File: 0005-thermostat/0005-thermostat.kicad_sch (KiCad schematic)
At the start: 41 parts, among them J1 EXT_NTC, J2 OUT, J3 PWR, J4 EXT_LED, J5 EXT_P1, J6 EXT_P2, P1 22k, P2 22k, T1 BC847B, T2 BC847B, T3 BC847B

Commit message: PCB enhancement
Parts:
- US1: footprint Package_DFN_QFN:DFN-8-1EP_2x2mm_P0.5mm_EP0.8x1.6mm -> Package_SO:SOP-8_3.76x4.96mm_P1.27mm
- US2: footprint Package_SO:TSSOP-14_4.4x5mm_P0.65mm -> Package_SO:SO-14_5.3x10.2mm_P1.27mm
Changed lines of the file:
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@@
 			)
 		)
-		(property "Footprint" "Package_SO:TSSOP-14_4.4x5mm_P0.65mm"
+		(property "Footprint" "Package_SO:SO-14_5.3x10.2mm_P1.27mm"
 			(at 138.43 100.33 0)
 			(hide yes)
@@
 			)
 		)
-		(property "Footprint" "Package_SO:TSSOP-14_4.4x5mm_P0.65mm"
+		(property "Footprint" "Package_SO:SO-14_5.3x10.2mm_P1.27mm"
 			(at 154.94 90.17 0)
 			(hide yes)
@@
 			)
 		)
-		(property "Footprint" "Package_DFN_QFN:DFN-8-1EP_2x2mm_P0.5mm_EP0.8x1.6mm"
+		(property "Footprint" "Package_SO:SOP-8_3.76x4.96mm_P1.27mm"
 			(at 100.33 102.87 0)
 			(hide yes)
@@
 			)
 		)
-		(property "Footprint" "Package_DFN_QFN:DFN-8-1EP_2x2mm_P0.5mm_EP0.8x1.6mm"
+		(property "Footprint" "Package_SO:SOP-8_3.76x4.96mm_P1.27mm"
 			(at 100.33 78.74 0)
 			(hide yes)
@@
 			)
 		)
-		(property "Footprint" "Package_DFN_QFN:DFN-8-1EP_2x2mm_P0.5mm_EP0.8x1.6mm"
+		(property "Footprint" "Package_SO:SOP-8_3.76x4.96mm_P1.27mm"
 			(at 158.75 152.4 0)
 			(hide yes)
@@
 			)
 		)
-		(property "Footprint" "Package_SO:TSSOP-14_4.4x5mm_P0.65mm"
+		(property "Footprint" "Package_SO:SO-14_5.3x10.2mm_P1.27mm"
 			(at 138.43 81.28 0)
 			(hide yes)
@@
 			)
 		)
-		(property "Footprint" "Package_SO:TSSOP-14_4.4x5mm_P0.65mm"
+		(property "Footprint" "Package_SO:SO-14_5.3x10.2mm_P1.27mm"
 			(at 172.72 90.17 0)
 			(hide yes)
@@
 			)
 		)
-		(property "Footprint" "Package_SO:TSSOP-14_4.4x5mm_P0.65mm"
+		(property "Footprint" "Package_SO:SO-14_5.3x10.2mm_P1.27mm"
 			(at 171.45 152.4 0)
 			(hide yes)

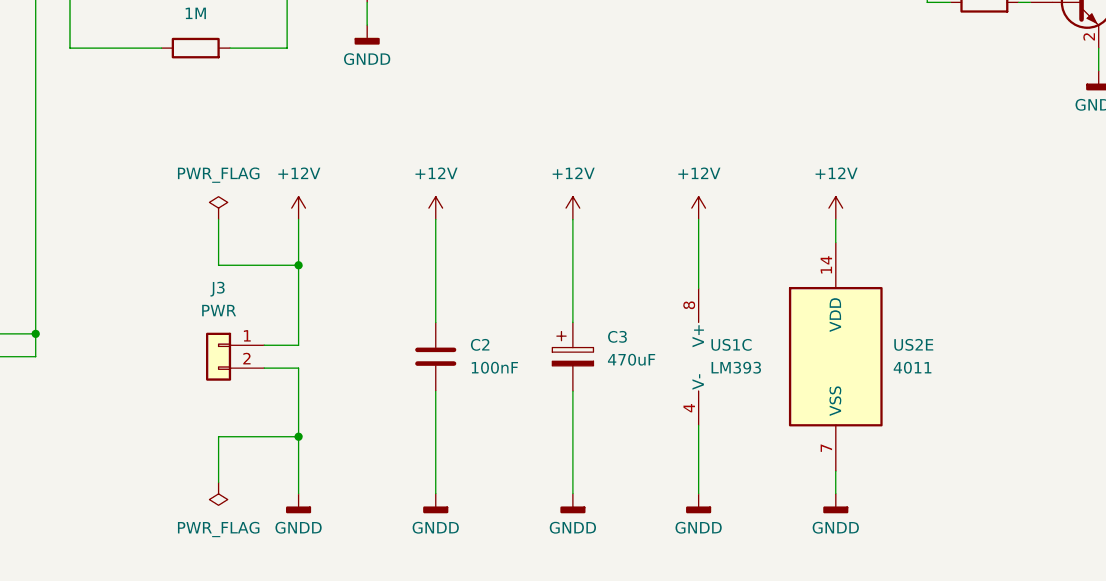
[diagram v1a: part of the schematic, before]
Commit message: Re-design comparator section, shrink the board
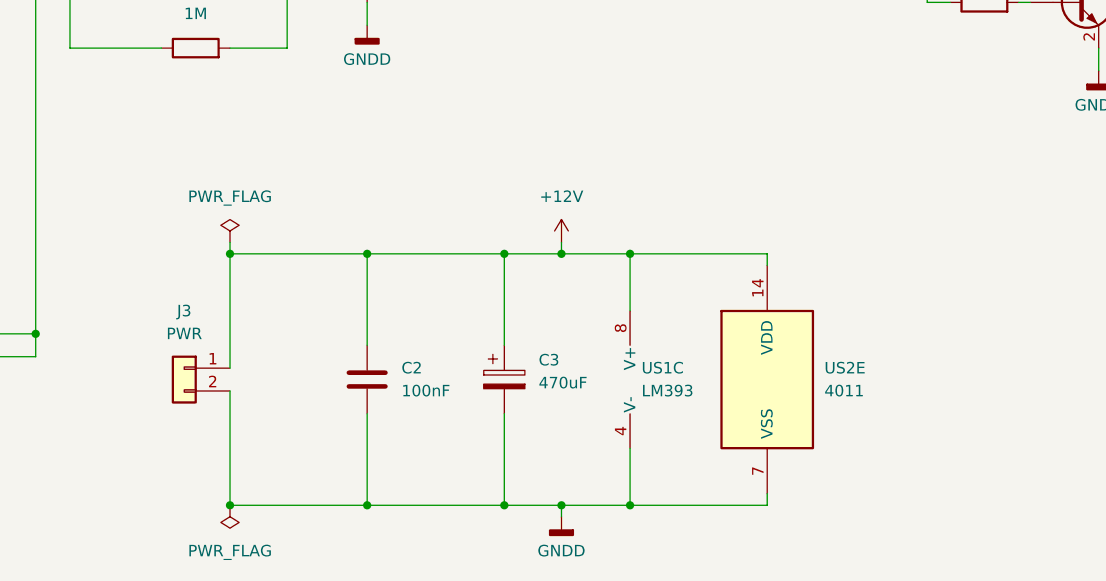
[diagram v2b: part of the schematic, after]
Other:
- moved on the sheet: C2, C3, J3, US1C, US2E

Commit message: Replace SOIC to TSSOP ICs footprints
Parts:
- US1: footprint Package_SO:SOP-8_3.76x4.96mm_P1.27mm -> Package_SO:TSSOP-8_4.4x3mm_P0.65mm
- US2: footprint Package_SO:SO-14_5.3x10.2mm_P1.27mm -> Package_SO:TSSOP-14_4.4x5mm_P0.65mm
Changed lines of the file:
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@@
 			)
 		)
-		(property "Footprint" "Package_SO:SO-14_5.3x10.2mm_P1.27mm"
+		(property "Footprint" "Package_SO:TSSOP-14_4.4x5mm_P0.65mm"
 			(at 138.43 100.33 0)
 			(hide yes)
@@
 			)
 		)
-		(property "Footprint" "Package_SO:SO-14_5.3x10.2mm_P1.27mm"
+		(property "Footprint" "Package_SO:TSSOP-14_4.4x5mm_P0.65mm"
 			(at 154.94 90.17 0)
 			(hide yes)
@@
 			)
 		)
-		(property "Footprint" "Package_SO:SOP-8_3.76x4.96mm_P1.27mm"
+		(property "Footprint" "Package_SO:TSSOP-8_4.4x3mm_P0.65mm"
 			(at 100.33 102.87 0)
 			(hide yes)
@@
 			)
 		)
-		(property "Footprint" "Package_SO:SOP-8_3.76x4.96mm_P1.27mm"
+		(property "Footprint" "Package_SO:TSSOP-8_4.4x3mm_P0.65mm"
 			(at 100.33 78.74 0)
 			(hide yes)
@@
 			)
 		)
-		(property "Footprint" "Package_SO:SOP-8_3.76x4.96mm_P1.27mm"
+		(property "Footprint" "Package_SO:TSSOP-8_4.4x3mm_P0.65mm"
 			(at 151.13 154.94 0)
 			(hide yes)
@@
 			)
 		)
-		(property "Footprint" "Package_SO:SO-14_5.3x10.2mm_P1.27mm"
+		(property "Footprint" "Package_SO:TSSOP-14_4.4x5mm_P0.65mm"
 			(at 138.43 81.28 0)
 			(hide yes)
@@
 			)
 		)
-		(property "Footprint" "Package_SO:SO-14_5.3x10.2mm_P1.27mm"
+		(property "Footprint" "Package_SO:TSSOP-14_4.4x5mm_P0.65mm"
 			(at 172.72 90.17 0)
 			(hide yes)
@@
 			)
 		)
-		(property "Footprint" "Package_SO:SO-14_5.3x10.2mm_P1.27mm"
+		(property "Footprint" "Package_SO:TSSOP-14_4.4x5mm_P0.65mm"
 			(at 163.83 154.94 0)
 			(hide yes)
